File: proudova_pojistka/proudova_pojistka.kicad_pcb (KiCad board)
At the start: 2 copper layers, 55 parts, among them J2 Pojistka, J3 Napájení +12V, Q1 Q_NMOS_GDS, Q2 BS170, Q5 BS170, Q6 BS170, Q7 BS170, SW1 ROZSAH, SW2 SW_Push, U3 LM311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

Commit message: Ready na konzultaci
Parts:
- moved R8 161.3 mm to (199.7, 122.0), turned to 180 degrees
- moved R9 161.1 mm to (199.5, 126.0), turned to 180 degrees
- moved C14 154.1 mm to (173.0, 124.0), turned to 180 degrees
- moved R10 153.4 mm to (192.1, 117.8)
- moved U3 151.8 mm to (180.9, 103.8), turned to 180 degrees
- moved R2 144.8 mm to (184.1, 92.2)
- moved R3 144.8 mm to (184.1, 96.3)
- moved R4 144.8 mm to (184.1, 100.3)
- moved R5 144.8 mm to (184.1, 104.4)
- moved R6 144.8 mm to (184.1, 108.5)
- moved R7 144.8 mm to (184.1, 112.5)
- moved C6 144.6 mm to (154.5, 118.0)
- moved C20 143.1 mm to (163.0, 139.5), turned to -90 degrees
- moved C12 143.1 mm to (165.1, 107.5)
- moved C13 143.1 mm to (165.1, 111.5)
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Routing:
- net GND: track 0.00 -> 404.1 mm, vias 0 -> 3
- net +12V: track 0.00 -> 189.3 mm, vias 0 -> 1
- net +5V: track 0.00 -> 104.5 mm
- net Net-(Q6-S): track 0.00 -> 96.0 mm, vias 0 -> 1
- net Net-(U6-Q): track 0.00 -> 84.1 mm
- net Net-(Q2-D): track 0.00 -> 64.1 mm
- net Net-(Q2-G): track 0.00 -> 54.4 mm, vias 0 -> 1
- net -10V: track 0.00 -> 48.3 mm
- net Net-(D6-A): track 0.00 -> 42.1 mm
- net Net-(U3-+): track 0.00 -> 41.6 mm
- net Net-(D3-K): track 0.00 -> 39.6 mm
- net Net-(R10-Pad1): track 0.00 -> 38.7 mm
- net Net-(U4--): track 0.00 -> 29.2 mm
- net Net-(C13-Pad2): track 0.00 -> 29.2 mm
- net Net-(Q1-S): track 0.00 -> 22.6 mm
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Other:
- board outline added: 89 x 64 mm
- board text added: "3 A 2,5 A 2 A 1,5 A 1 A 0,75 A 0,5 A 0,25 A"
- board text added: "Elektronická proudová pojistka"

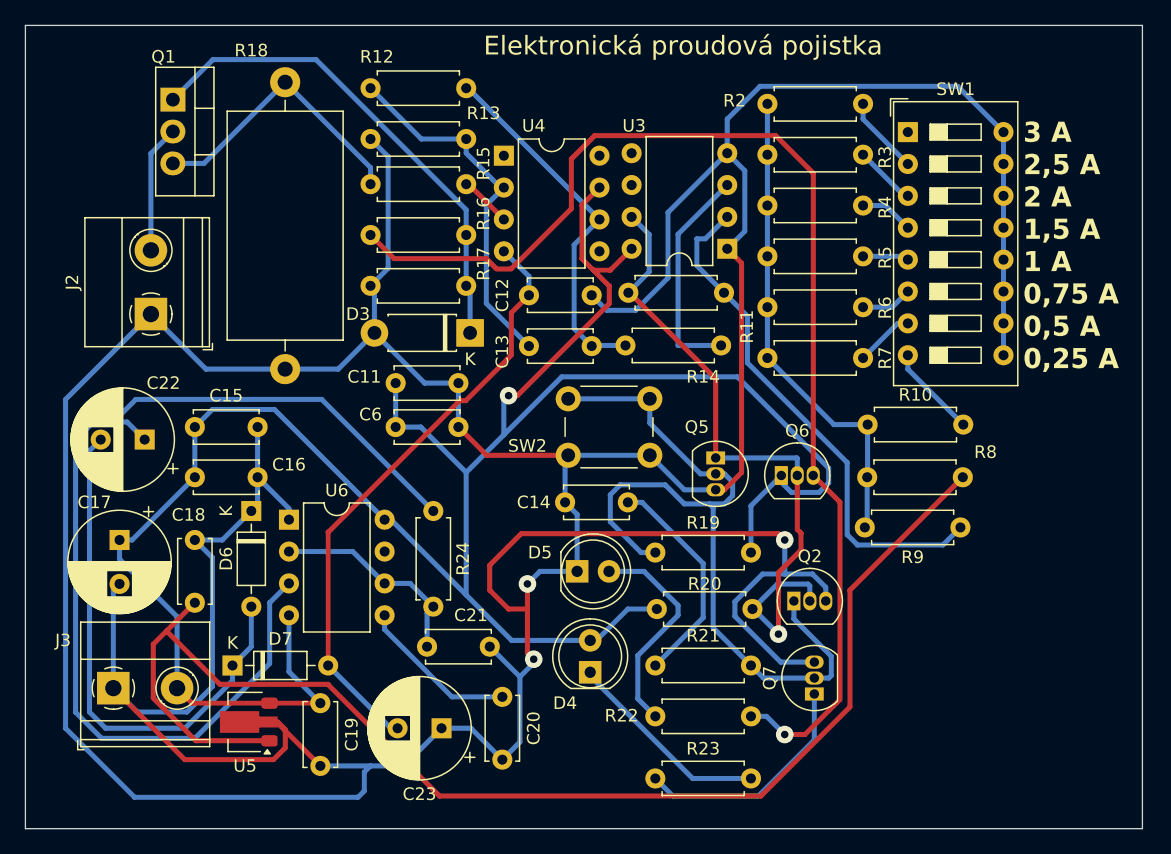
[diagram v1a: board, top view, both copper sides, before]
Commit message: Odevzdaná verze - Přidaný ground plane
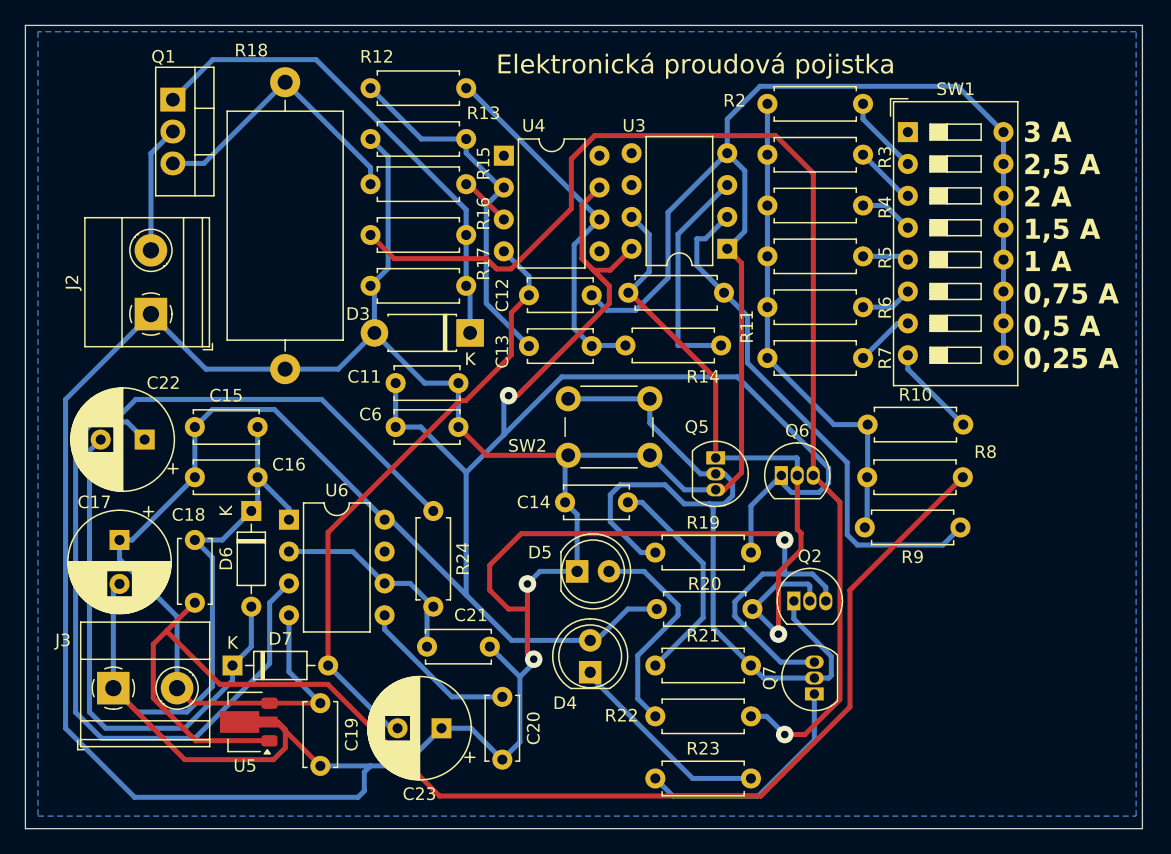
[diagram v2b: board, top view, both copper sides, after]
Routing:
- added copper zone on B.Cu, net GND
